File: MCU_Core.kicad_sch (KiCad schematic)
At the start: 16 parts, among them U1 STM32F405RGTx

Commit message: Update SCH
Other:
- moved on the sheet: C1, C2, C3, R1, R11, R2, R3, S1

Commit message: Update SCH
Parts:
- renumbered C4 to C1, C5 to C2, C6 to C3, C7 to C4, C8 to C5, C9 to C6, C1 to C7, C2 to C8, C3 to C9, R11 to R2, R2 to R4
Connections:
- net SPI2_MISO: now reaches U1.10 (PC2)
- net SPI2_MOSI: now reaches U1.11 (PC3)
- net SPI1_CS: now reaches U1.20 (PA4)
- net SPI1_SCK: now reaches U1.21 (PA5)
- net SPI1_MISO: now reaches U1.22 (PA6)
- net SPI1_MOSI: now reaches U1.23 (PA7)
- net SPI2_CS: now reaches U1.33 (PB12)
- net SPI2_SCK: now reaches U1.34 (PB13)
- net SPI3_CS: now reaches U1.50 (PA15)
- net SPI3_SCK: now reaches U1.55 (PB3)
- net SPI3_MISO: now reaches U1.56 (PB4)
- net SPI3_MOSI: now reaches U1.57 (PB5)
- net BARO_SCL: now reaches U1.58 (PB6)
- net BARO_SDA: now reaches U1.59 (PB7)

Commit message: Finished SCH
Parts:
- added D4, D5: LED, LED_SMD:LED_0603_1608Metric, symbol Device:LED
- added R25, R26: 100R, Resistor_SMD:R_0402_1005Metric, symbol Library:R
- C1, C2, C3, C4, C5, C6, C7, C8, C9: footprint (none) -> Capacitor_SMD:C_0402_1005Metric
- L1: footprint (none) -> Inductor_SMD:L_0603_1608Metric
- R1: footprint (none) -> Resistor_SMD:R_0402_1005Metric
- R2, R3: footprint Resistor_SMD:R_0603_1608Metric -> Resistor_SMD:R_0402_1005Metric
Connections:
- net +3.3V: now also R25.2, R26.2
- net USART4_TX: now reaches U1.14 (PA0)
- net USART4_RX: now reaches U1.15 (PA1)
- net USART2_TX: now reaches U1.16 (PA2)
- net USART2_RX: now reaches U1.17 (PA3)
- net LED1: now reaches U1.2 (PC13)
- net LED1: now also D4.1 (K)
- net ADC_RSSI: now reaches U1.25 (PC5)
- net MOTOR3: now reaches U1.26 (PB0)
- net MOTOR4: now reaches U1.27 (PB1)
- net MOTOR1: now reaches U1.29 (PB10)
- net LED2: now reaches U1.3 (PC14)
- net LED2: now also D5.1 (K)
- net MOTOR2: now reaches U1.30 (PB11)
- net GYRO_CLK: now reaches U1.36 (PB15)
- net USART6_TX: now reaches U1.37 (PC6)
- net USART6_RX: now reaches U1.38 (PC7)
- net LED_STRIP: now reaches U1.39 (PC8)
- net I2C3_SDA: now reaches U1.40 (PC9)
- net I2C3_SCL: now reaches U1.41 (PA8)
- net USART1_RX: now reaches U1.43 (PA10)
- net USB_DN: now reaches U1.44 (PA11)
- net USB_DP: now reaches U1.45 (PA12)
- net SWDIO: now reaches U1.46 (PA13)
- net SWCLK: now reaches U1.49 (PA14)
- net USART3_TX: now reaches U1.51 (PC10)
- net USART3_RX: now reaches U1.52 (PC11)
- net USART5_RX: now reaches U1.54 (PD2)
- net CAMERA_CTRL: now reaches U1.61 (PB8)
- net BEEPER: now reaches U1.62 (PB9)
- net ADC_VBAT: now reaches U1.8 (PC0)
- net ADC_CURR: now reaches U1.9 (PC1)
- new net: D5.2 (A), R26.1
- new net: D4.2 (A), R25.1
- no-connect marks 0 -> 5
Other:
- moved on the sheet: C7, C8, C9, R1, R2, R3, R4, S1, U1

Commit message: Updated PCB Layout
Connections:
- net VTX_PW_SW: now reaches U1.4 (PC15)
- no-connect marks 5 -> 4
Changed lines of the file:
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@@
-	)
-	(no_connect
-		(at 41.91 101.6)
 	)
 	(no_connect
@@
 		(pts
 			(xy 30.48 76.2) (xy 41.91 76.2)
+		)
+		(stroke
+			(width 0)
+			(type default)
+		)
+	)
+	(wire
+		(pts
+			(xy 30.48 101.6) (xy 41.91 101.6)
 		)
 		(stroke
@@
 				(hide yes)
 			)
+		)
+	)
+	(global_label "VTX_PW_SW"
+		(shape input)
+		(at 30.48 101.6 180)
+		(fields_autoplaced yes)
+		(effects
+			(font
+				(size 1.27 1.27)
+			)
+			(justify right)
+		)
+		(property "Intersheetrefs" "${INTERSHEET_REFS}"
+			(at 17.7581 101.6 0)
+			(effects
+				(font
+					(size 1.27 1.27)
+				)
+				(justify right)
+				(hide yes)
+			)

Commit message: Update PCB Layout
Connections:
- net +3.3V is gone; now on net +3.3V_MCU: R25.2, R26.2, S1.2 (A)
- net BARO_SCL renamed I2C1_SCL
- net BARO_SDA renamed I2C1_SDA
- net I2C3_SCL: no longer names the net of U1.41 (PA8)
- net I2C3_SDA renamed SERVO2
- net LED_STRIP renamed SERVO1
- no-connect marks 4 -> 5

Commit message: Updated PCB Layout
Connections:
- net LED_STRIP: now reaches U1.41 (PA8)
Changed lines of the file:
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@@
 	)
 	(no_connect
-		(at 82.55 60.96)
+		(at 82.55 63.5)
 	)
 	(no_connect
@@
 		(pts
 			(xy 25.4 157.48) (xy 25.4 158.75)
+		)
+		(stroke
+			(width 0)
+			(type default)
+		)
+	)
+	(wire
+		(pts
+			(xy 82.55 60.96) (xy 91.44 60.96)
 		)
 		(stroke
@@
 			(effects
 				(font
+					(size 1.27 1.27)
+				)
+				(justify left)
+				(hide yes)
+			)
+		)
+	)
+	(global_label "LED_STRIP"
+		(shape input)
+		(at 91.44 60.96 0)
+		(fields_autoplaced yes)
+		(effects
+			(font
+				(size 1.27 1.27)
+			)
+			(justify left)
+		)
+		(property "Intersheetrefs" "${INTERSHEET_REFS}"
+			(at 103.3757 60.96 0)
+			(effects
+				(font

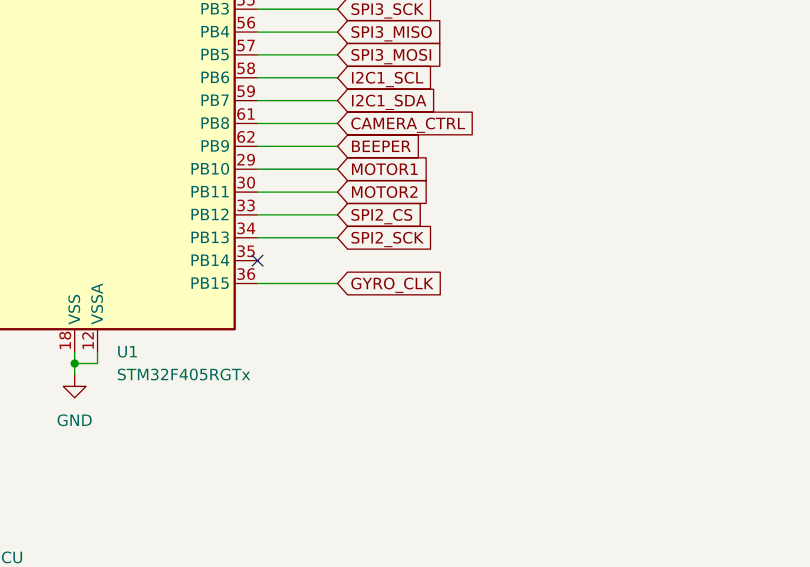
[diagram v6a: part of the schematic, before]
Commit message: Finished PCB SilkScreen V1.0
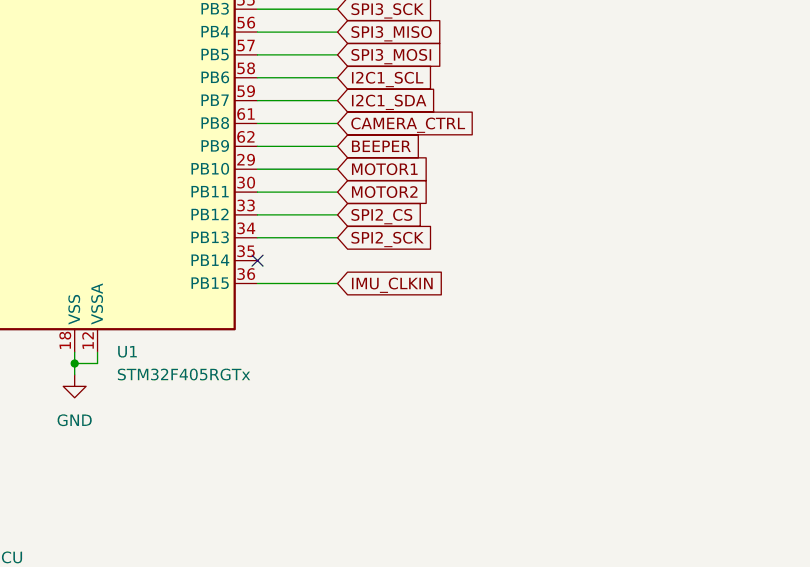
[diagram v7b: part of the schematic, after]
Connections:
- net GYRO_CLK renamed IMU_CLKIN
